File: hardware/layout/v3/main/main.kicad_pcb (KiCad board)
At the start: 4 copper layers, 39.8 x 76.8 mm, 39 parts, among them J1 KNX bus (red/black), J2 AUX 20-32 V (yellow/white), J3 UI board, J4 KNX board, J5 DALI logic, J6 DALI bus, Q1 MJD45H11, Q2 BC857, U1 SCT2400TVBR, U2 REM3-2415S/A/CTRL 24V->15V 3W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, U3 TLP383, U4 LM66100, U5 XIAO ESP32C6

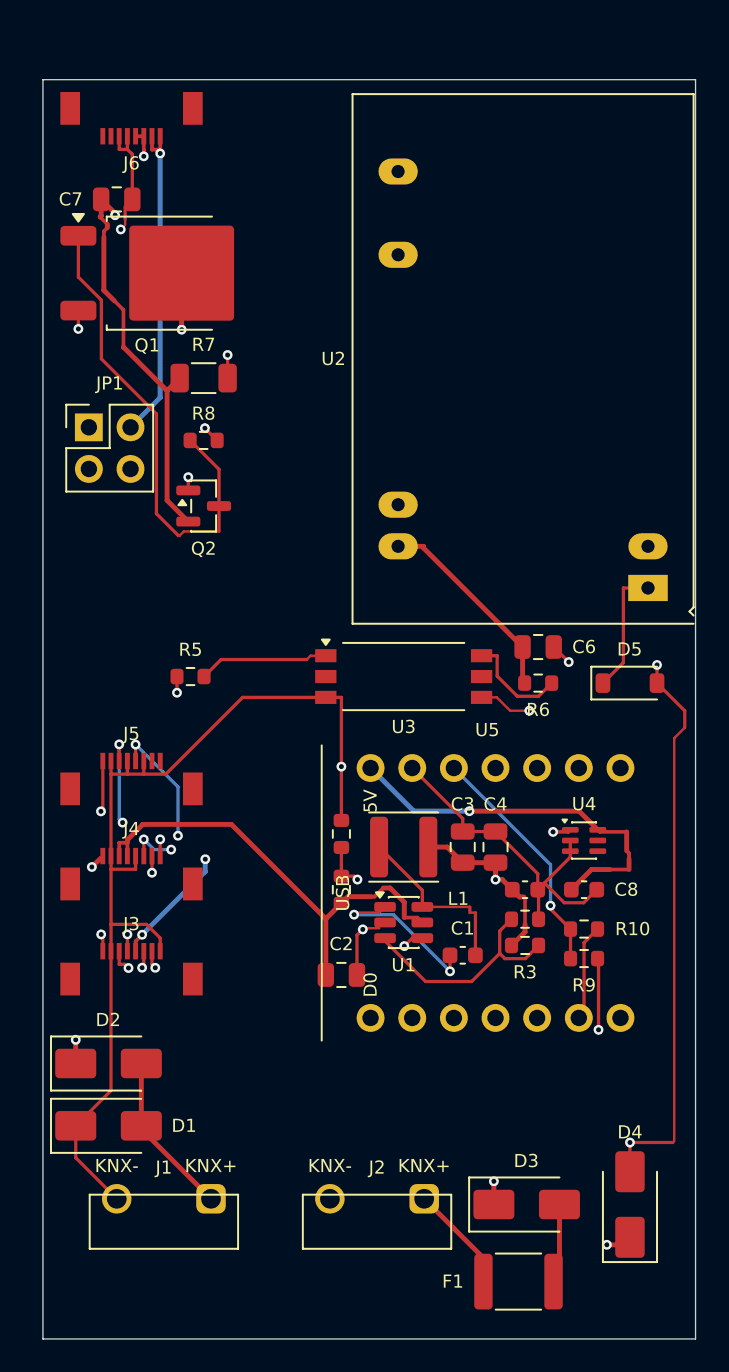
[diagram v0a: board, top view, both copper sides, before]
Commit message: V3 consolidated to two boards (main + ui); updated firmware pin map, button ADC, and OLED connector; removed separate knx/dali boards from CI matrix
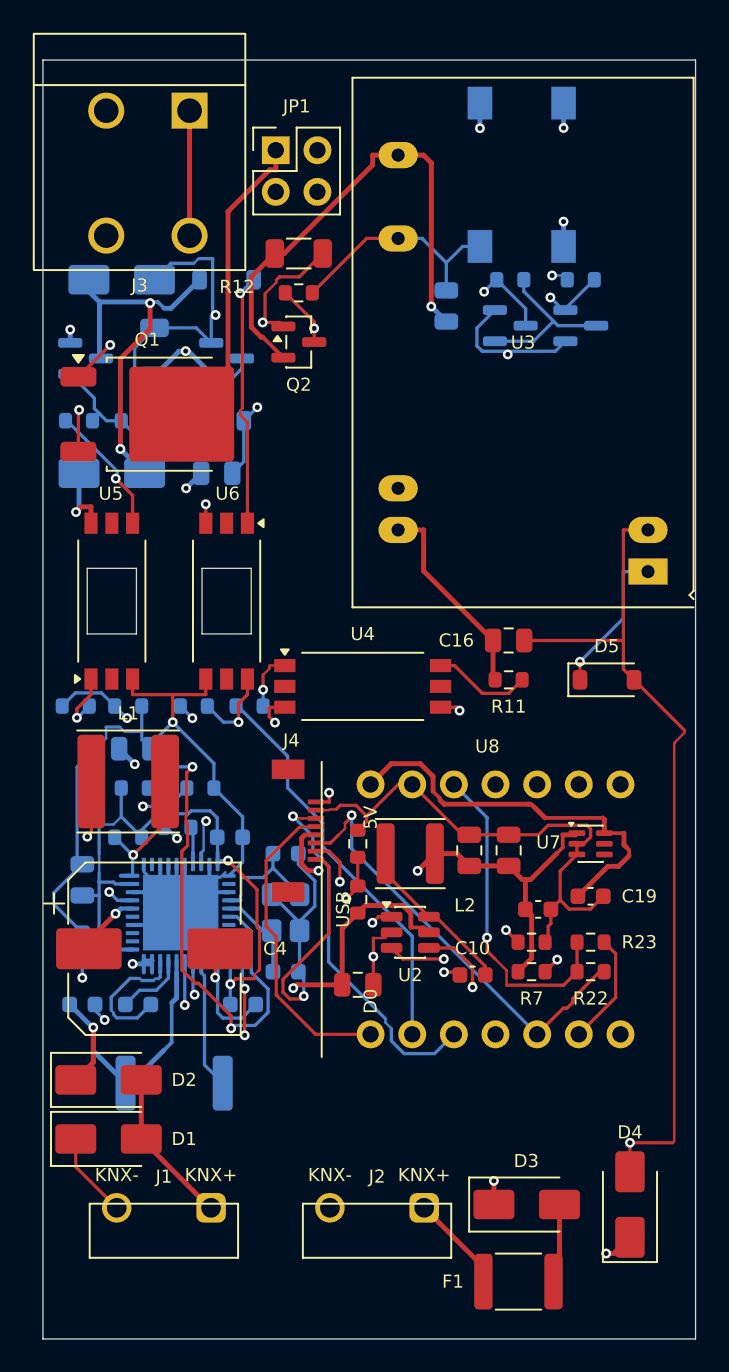
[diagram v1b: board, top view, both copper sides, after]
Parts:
- removed J5: DALI logic, gateway_fp:FPC_Kinghelm_KH-FPC0.5-H1.2SMT-8P
- removed J6: DALI bus, gateway_fp:FPC_Kinghelm_KH-FPC0.5-H1.2SMT-8P
- added C10: 100n 50V, Capacitor_SMD:C_0603_1608Metric, F.Cu at (26.2, -22.2)
- added C11: 10u 50V, Capacitor_SMD:C_0805_2012Metric, F.Cu at (19.2, -21.6)
- added C12: 22u 25V, Capacitor_SMD:C_0805_2012Metric, F.Cu at (26.0, -29.8)
- added C13: 22u 25V, Capacitor_SMD:C_0805_2012Metric, F.Cu at (28.4, -29.8)
- added C14: 100n 50V, Capacitor_SMD:C_0603_1608Metric, F.Cu at (30.2, -26.2)
- added C15: 1u 50V, Capacitor_SMD:C_0805_2012Metric, B.Cu at (5.60, -36.0)
- added C16: 10u 50V, Capacitor_SMD:C_0805_2012Metric, F.Cu at (28.4, -42.6)
- added C17: 10u 25V, Capacitor_SMD:C_0805_2012Metric, B.Cu at (24.6, -63.0)
- added C18: 1u 50V, Capacitor_SMD:C_0805_2012Metric, B.Cu at (10.6, -52.8)
- added C19: 10u 10V, Capacitor_SMD:C_0603_1608Metric, F.Cu at (33.4, -27.0)
- added C9: 18p C0G 50V, Capacitor_SMD:C_0603_1608Metric, B.Cu at (14.8, -29.6)
- added D10: 5V6, Diode_SMD:D_SOD-123, B.Cu at (11.2, -64.6)
- added D6: DF06S, Diode_SMD:Diode_Bridge_Vishay_DFS, B.Cu at (29.2, -71.0)
- added D7: SMAJ24A, Diode_SMD:D_SMA, B.Cu at (4.80, -64.6)
- added D8: SS16, Diode_SMD:D_SMA, B.Cu at (4.20, -52.8)
- added D9: 12V, Diode_SMD:D_SOD-123, B.Cu at (10.6, -56.0)
- added L2: 4.7uH, Inductor_SMD:L_APV_ANR4012, F.Cu at (22.4, -29.6)
- added Q3: IRLML0060, Package_TO_SOT_SMD:SOT-23, B.Cu at (2.60, -59.8)
- added Q4: BC847, Package_TO_SOT_SMD:SOT-23, B.Cu at (11.2, -59.8)
- added Q5: BC847, Package_TO_SOT_SMD:SOT-23, B.Cu at (28.5, -61.8)
- added Q6: BC847, Package_TO_SOT_SMD:SOT-23, B.Cu at (32.8, -61.8)
- added R11: 10k, Resistor_SMD:R_0603_1608Metric, F.Cu at (28.4, -40.2)
- added R12: 3R3, Resistor_SMD:R_1206_3216Metric, F.Cu at (15.6, -66.2)
- added R13: 4k7, Resistor_SMD:R_0603_1608Metric, F.Cu at (15.6, -63.8)
- added R14: 330R, Resistor_SMD:R_0603_1608Metric, B.Cu at (2.00, -38.6)
- added R15: 10k, Resistor_SMD:R_0603_1608Metric, B.Cu at (5.20, -38.6)
- added R16: 22k, Resistor_SMD:R_0603_1608Metric, B.Cu at (2.20, -56.0)
- added R17: 100k, Resistor_SMD:R_0603_1608Metric, B.Cu at (5.60, -56.0)
- added R18: 3R3, Resistor_SMD:R_1206_3216Metric, B.Cu at (6.80, -60.2)
- added R19: 100k, Resistor_SMD:R_0603_1608Metric, B.Cu at (28.5, -64.6)
- added R20: 680R, Resistor_SMD:R_0603_1608Metric, B.Cu at (32.8, -64.6)
- added R21: 10k, Resistor_SMD:R_0603_1608Metric, B.Cu at (9.20, -38.6)
- added R22: 4k7, Resistor_SMD:R_0603_1608Metric, F.Cu at (33.4, -22.4)
- added R23: 4k7, Resistor_SMD:R_0603_1608Metric, F.Cu at (33.4, -24.2)
- added U6: TLP383(D4BLLTL,E, Package_SO:SO-6L_10x3.84mm_P1.27mm, F.Cu at (11.2, -45.0)
- added U7: LM66100, Package_TO_SOT_SMD:SOT-363_SC-70-6, F.Cu at (33.4, -30.2)
- added U8: XIAO ESP32C6, gateway_fp:XIAO_ESP32C6_Header, F.Cu at (27.6, -26.2)
- added Y1: 16MHz, Crystal:Crystal_SMD_3225-4Pin_3.2x2.5mm, B.Cu at (14.8, -26.0)
- C1: value 100n 50V -> 47n 50V; moved to B.Cu
- C2, C6: value 10u 50V -> 100n 50V; footprint Capacitor_SMD:C_0805_2012Metric -> Capacitor_SMD:C_0603_1608Metric; moved to B.Cu
- C3: value 22u 25V -> 220n 50V; footprint Capacitor_SMD:C_0805_2012Metric -> Capacitor_SMD:C_0603_1608Metric; moved to B.Cu
- C4: value 22u 25V -> 470u 35V; footprint Capacitor_SMD:C_0805_2012Metric -> Capacitor_SMD:CP_Elec_10x10
- C5: moved to B.Cu
- C7: value 10u 25V -> 22u 25V; moved to B.Cu
- C8: value 10u 10V -> 18p C0G 50V; moved to B.Cu
- J1: value KNX bus (red/black) -> KNX bus terminal pins
- J3: value UI board -> DALI bus (push-in); footprint gateway_fp:FPC_Kinghelm_KH-FPC0.5-H1.2SMT-8P -> gateway_fp:TerminalBlock_Kefa_KF142R-5.08-2P
- J4: value KNX board -> UI board
- L1: value 4.7uH -> 220uH; footprint Inductor_SMD:L_APV_ANR4012 -> Inductor_SMD:L_Sunlord_SWPA6045S
- R1: value 120k 1% -> 10k 1%; moved to B.Cu
- R10: value 4k7 -> 330R; moved to B.Cu
- R2: value 10k 1% -> 10k; moved to B.Cu
- R3: value 51k 1% -> 27R; footprint Resistor_SMD:R_0603_1608Metric -> Resistor_SMD:R_2512_6332Metric; moved to B.Cu
- R4: value 10k 1% -> 1R; moved to B.Cu
- R5: value 330R -> 120k 1%
- R6: value 10k -> 10k 1%
- R7: value 3R3 -> 51k 1%; footprint Resistor_SMD:R_1206_3216Metric -> Resistor_SMD:R_0603_1608Metric
- R8: value 4k7 -> 10k 1%
- R9: value 4k7 -> 1k; moved to B.Cu
- U1: value SCT2400TVBR -> NCN5130MNTWG; footprint Package_TO_SOT_SMD:TSOT-23-6 -> Package_DFN_QFN:QFN-40-1EP_6x6mm_P0.5mm_EP4.6x4.6mm; moved to B.Cu
- U2: value REM3-2415S/A/CTRL 24V->15V 3W iso -> SCT2400TVBR; footprint gateway_fp:Converter_DCDC_RECOM_REM3_DIP24_CTRL -> Package_TO_SOT_SMD:TSOT-23-6
- U3: value TLP383 -> REM3-2415S/A/CTRL 24V->15V 3W iso; footprint Package_SO:SO-6L_10x3.84mm_P1.27mm -> gateway_fp:Converter_DCDC_RECOM_REM3_DIP24_CTRL
- U4: value LM66100 -> TLP383; footprint Package_TO_SOT_SMD:SOT-363_SC-70-6 -> Package_SO:SO-6L_10x3.84mm_P1.27mm
- U5: value XIAO ESP32C6 -> TLP383(D4BLLTL,E; footprint gateway_fp:XIAO_ESP32C6_Header -> Package_SO:SO-6L_10x3.84mm_P1.27mm
- moved J3 48.3 mm to (6.40, -71.1), turned to 180 degrees
- moved C7 41.6 mm to (2.40, -28.0), turned to 90 degrees
- moved R7 41.4 mm to (29.8, -22.4)
- moved R8 36.6 mm to (29.8, -24.2)
- moved U5 29.4 mm to (4.20, -45.0)
- moved R9 26.1 mm to (8.20, -31.2)
- moved U2 25.5 mm to (22.4, -24.8), turned to 0 degrees
- moved R4 24.7 mm to (5.20, -30.6)
- moved R10 24.5 mm to (12.6, -38.6)
- moved C1 23.4 mm to (2.40, -20.4)
- moved R3 23.0 mm to (8.00, -15.6)
- moved C6 22.1 mm to (11.4, -30.6)
- moved C3 22.0 mm to (5.80, -20.4), turned to 0 degrees
- moved C4 21.7 mm to (6.80, -23.8), turned to 0 degrees
- moved JP1 20.4 mm to (14.2, -72.5)
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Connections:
- C1 pad 1: N$2 -> KNX_P_PROT
- C1 pad 2: BUCK5_SW -> CCP
- C2 pad 1: VFILT -> CAV
- C3 pad 1: +5V -> CEQ1
- C3 pad 2: GND -> CEQ2
- C4 pad 1: +5V -> VFILT
- C5 pad 1: +5V -> +3V3_TRX
- C6 pad 1: AUX_P -> +3V3_TRX
- C6 pad 2: GNDA -> GND
- C7 pad 1: DALI_ISO15V -> +3V3_TRX
- C7 pad 2: GNDD -> GND
- C8 pad 1: +5V_XIAO -> XTAL1
- D5 pad 1: N$6 -> N$7
- J3 pad 1: +3V3 -> DA1
- J3 pad 2: GND -> DA2
- J4 pad 1: KNX_P_PROT -> +3V3
- J4 pad 3: VFILT -> BTN_LADDER
- J4 pad 4: VFILT -> LED_DATA
- J4 pad 5: GND -> +5V
- J4 pad 6: KNX_TXD -> I2C_SDA
- J4 pad 7: KNX_RXD -> I2C_SCL
- J4 pad 8: NCN_SAVEB -> GND
- L1 pad 1: BUCK5_SW -> VSW1
- L1 pad 2: +5V -> VDD1M
- Q1 pad 1: N$8 -> N$9
- Q1 pad 3: N$7 -> N$8
- Q2 pad 1: N$7 -> N$8
- Q2 pad 3: N$8 -> N$9
- R1 pad 1: VFILT -> FANIN
- R1 pad 2: N$1 -> GND
- R10 pad 1: +3V3 -> DALI_SUPPLY_OFF
- R10 pad 2: I2C_SCL -> N$5
- R2 pad 1: N$1 -> +3V3_TRX
- R2 pad 2: GND -> NCN_SAVEB
- R3 pad 1: +5V -> KNX_P_PROT
- R3 pad 2: N$3 -> TX0
- R4 pad 1: N$3 -> VDD1M
- R4 pad 2: GND -> +3V3_TRX
- R5 pad 1: DALI_SUPPLY_OFF -> VFILT
- R5 pad 2: N$4 -> N$1
- R6 pad 1: AUX_P -> N$1
- R6 pad 2: N$5 -> GND
- R7 pad 1: DALI_ISO15V -> +5V
- R7 pad 2: N$7 -> N$3
- R8 pad 1: N$8 -> N$3
- R8 pad 2: GNDD -> GND
- R9 pad 1: +3V3 -> KNX_RXD
- R9 pad 2: I2C_SDA -> N$4
- U1 pad 1: N$2 -> GND
- U1 pad 3: N$3 -> TX0
- U1 pad 4: N$1 -> CCP
- U1 pad 5: VFILT -> CAV
- U1 pad 6: BUCK5_SW -> KNX_P_PROT
- U2 pad 1: N$6 -> N$2
- U2 pad 2: GNDA -> GND
- U3 pad 1: N$4 -> N$7
- U3 pad 2: (no net) -> GNDA
- U4 pad 1: +5V -> N$5
- U4 pad 2: GND -> (no net)
- U4 pad 4: (no net) -> N$7
- U4 pad 6: +5V_XIAO -> N$6
- U5 pad 1: LED_DATA -> N$10
- U5 pad 2: DALI_SUPPLY_OFF -> (no net)
- U5 pad 3: BTN_LADDER -> GND
- U5 pad 4: LED_DALI -> DALI_GATE_SW
- U5 pad 5: I2C_SDA -> (no net)
- U5 pad 6: I2C_SCL -> DALI_BOOT
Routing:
- net DA_P: track 0.00 -> 52.7 mm, vias 0 -> 3
- net GND: track 90.0 -> 138.9 mm, vias 2 -> 5
- net +3V3_TRX: track 0.00 -> 39.5 mm, vias 0 -> 2
- net FANIN: track 0.00 -> 39.0 mm, vias 0 -> 3
- net RX_LIM_IN: track 0.00 -> 31.2 mm, vias 0 -> 2
- net NCN_SAVEB: track 25.8 -> 54.4 mm, vias 1 -> 2
- net N$9: track 0.00 -> 23.4 mm, vias 0 -> 2
- net DALI_SUPPLY_OFF: track 41.8 -> 24.5 mm, vias 1 -> 0
- net VFILT: track 28.7 -> 45.8 mm, vias 0 -> 4
- net GNDD: track 25.0 -> 41.9 mm, vias 2 -> 3
- net N$6: track 22.6 -> 6.02 mm, vias 1 -> 0
- net N$12: track 0.00 -> 16.0 mm, vias 0 -> 2
- net N$11: track 0.00 -> 15.5 mm, vias 0 -> 1
- net DALI_GATE: track 0.00 -> 15.2 mm
- net GNDA: track 35.7 -> 50.9 mm, vias 3 -> 1
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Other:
- board size 39.8 x 76.8 mm -> 39.8 x 78 mm

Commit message: README, hardware docs, and clangd config updates: expanded V3 details with REM3 supply control, isolation specs, and 1-DIN assembly; added system include resolution to compiledb script; updated variants table with all three releases
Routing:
- net GND: track 138.9 -> 139.6 mm
